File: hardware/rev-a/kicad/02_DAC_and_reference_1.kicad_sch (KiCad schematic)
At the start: 16 parts, among them U1 MCP4922-E/P, U2 MCP4922-E/P, U3 MCP4922-E/P, U4 MCP1501-20E/CHY

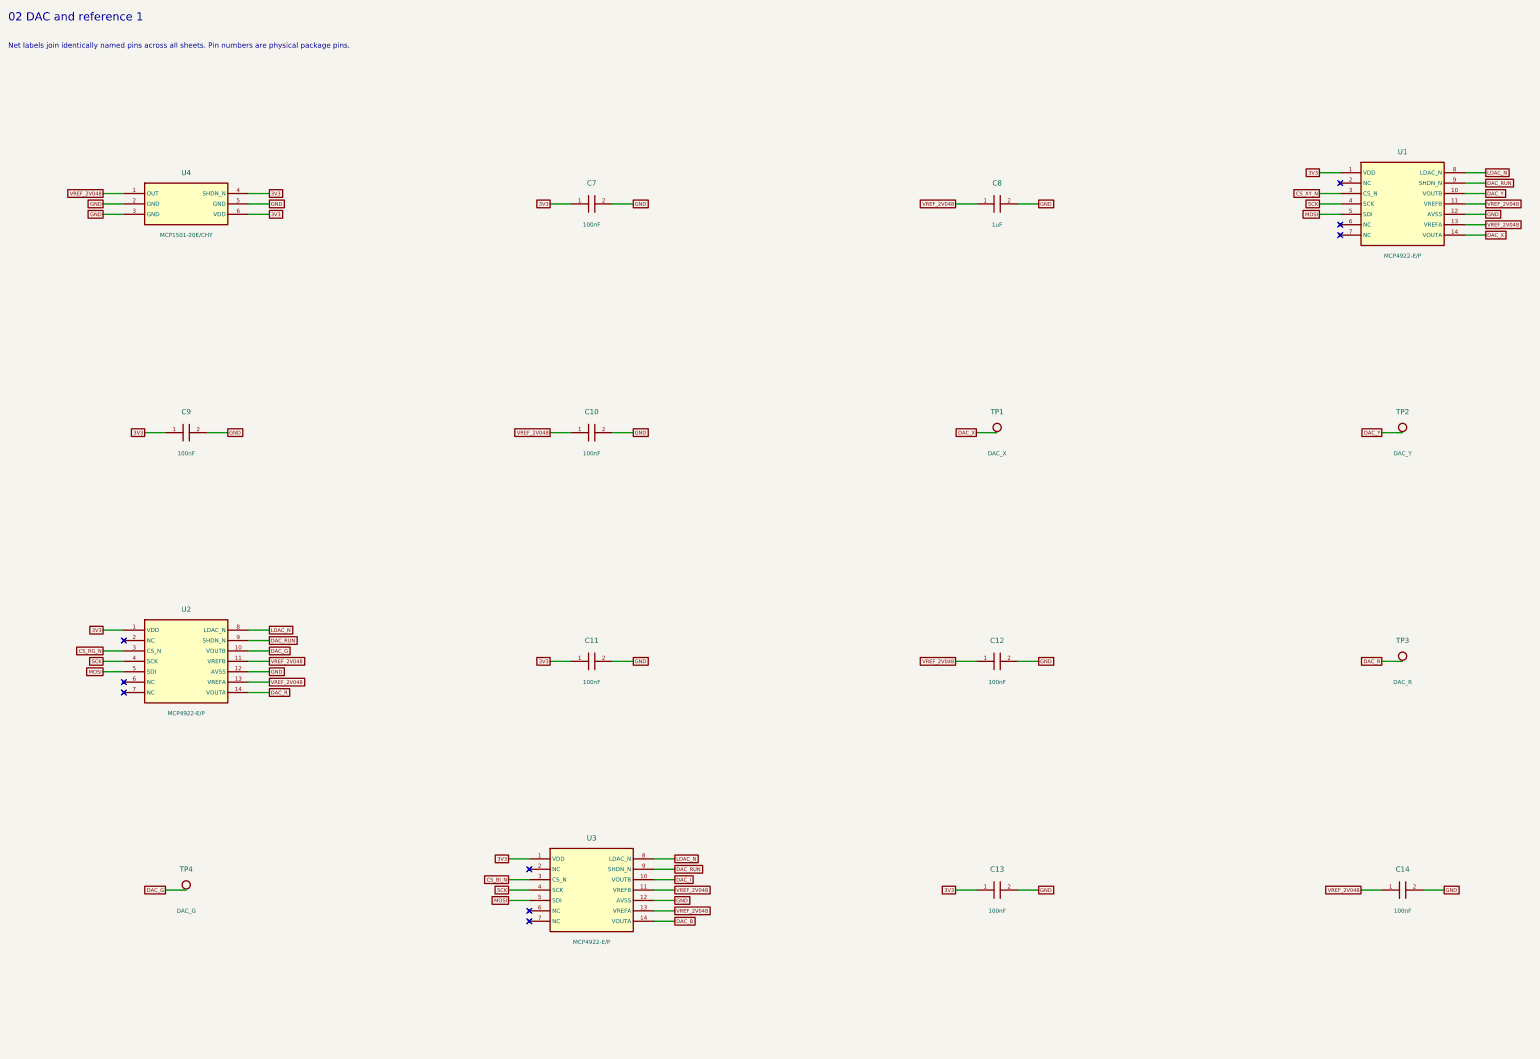
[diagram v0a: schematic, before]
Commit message: Redraw Rev.A schematics with functional blocks and explicit wiring
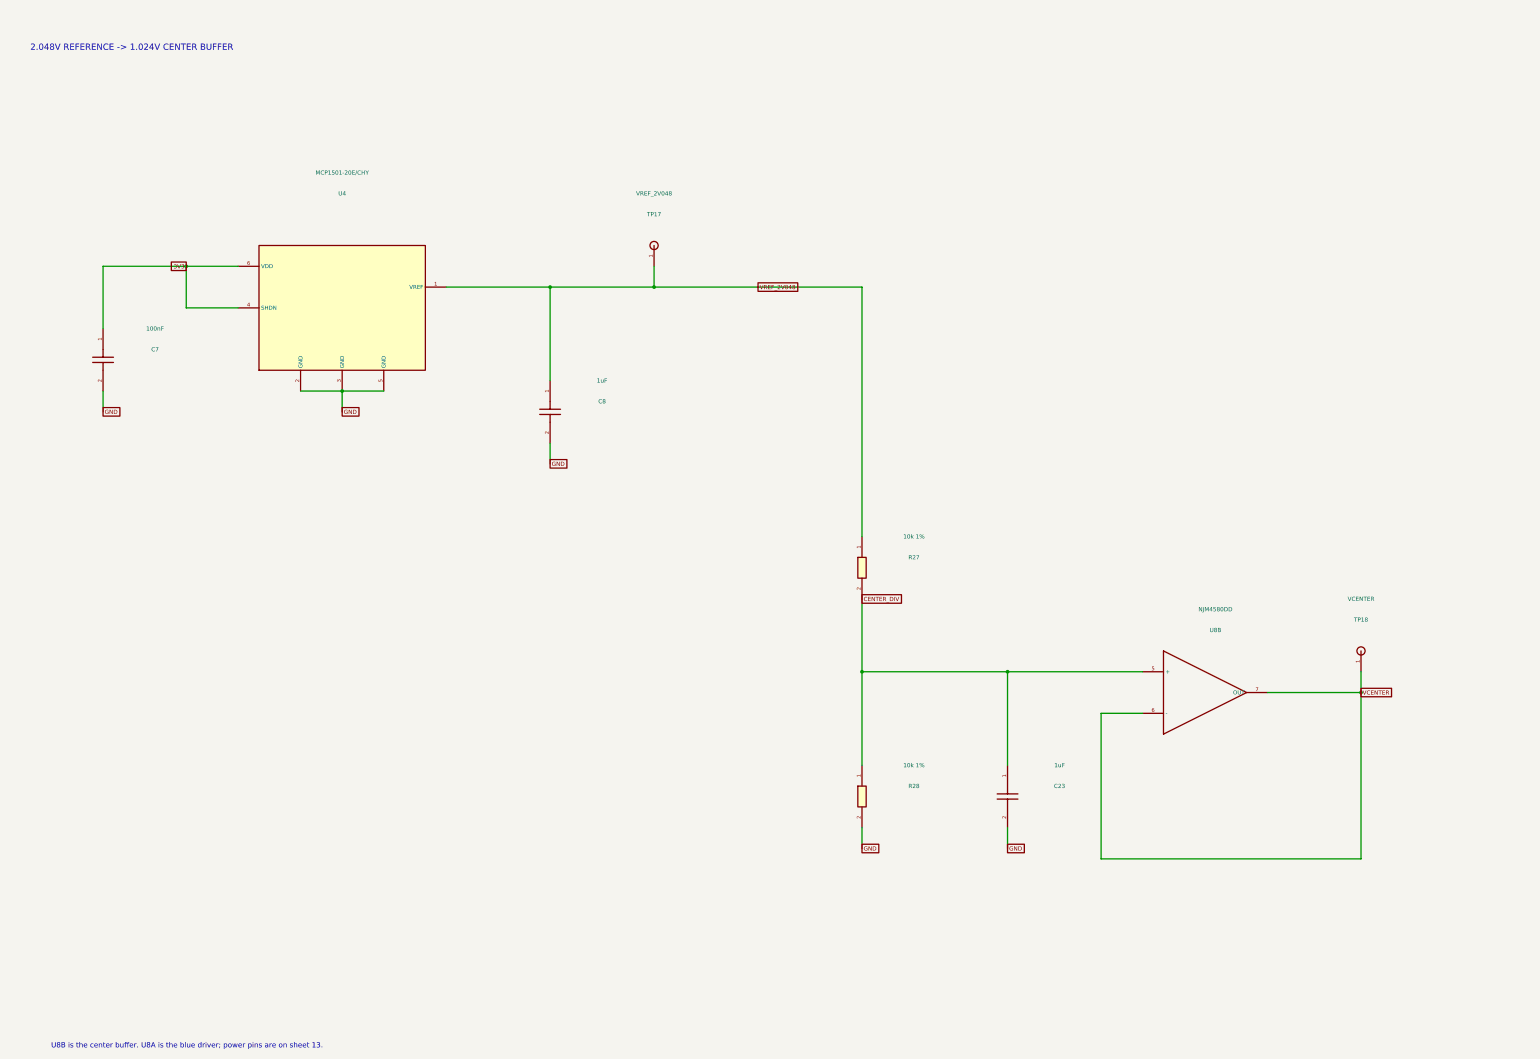
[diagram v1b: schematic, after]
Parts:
- removed C10, C11, C12, C13, C14, C9: 100nF, RevA:C_Disc_D5.0mm_W2.5mm_P5.00mm, symbol RevA:C
- removed TP1: DAC_X, RevA:TestPoint_THTPad_D2.0mm_Drill1.0mm, symbol RevA:TP
- removed TP2: DAC_Y, RevA:TestPoint_THTPad_D2.0mm_Drill1.0mm, symbol RevA:TP
- removed TP3: DAC_R, RevA:TestPoint_THTPad_D2.0mm_Drill1.0mm, symbol RevA:TP
- removed TP4: DAC_G, RevA:TestPoint_THTPad_D2.0mm_Drill1.0mm, symbol RevA:TP
- removed U1, U2, U3: MCP4922-E/P, RevA:DIP-14_W7.62mm, symbol RevA:DAC
- added C23: 1uF, RevA:C_Disc_D5.0mm_W2.5mm_P5.00mm, symbol RevA:C
- added R27, R28: 10k 1%, RevA:R_Axial_DIN0207_L6.3mm_D2.5mm_P10.16mm_Horizontal, symbol RevA:R
- added TP17: VREF_2V048, RevA:TestPoint_THTPad_D2.0mm_Drill1.0mm, symbol RevA:TP
- added TP18: VCENTER, RevA:TestPoint_THTPad_D2.0mm_Drill1.0mm, symbol RevA:TP
- added U8: NJM4580DD, RevA:DIP-8_W7.62mm, symbol RevA:AMP
- U4: symbol RevA:VREF -> RevA:Part_U4
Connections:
- net GND: now also C23.2, R28.2
- net VREF_2V048: now also R27.1, TP17.1
- new net CENTER_DIV: C23.1, R27.2, R28.1, U8.5 (+)
- new net VCENTER: TP18.1, U8.6 (-), U8.7 (OUT)
- no-connect marks 9 -> 0
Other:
- note added: "2.048V REFERENCE -> 1.024V CENTER BUFFER"
- note added: "U8B is the center buffer. U8A is the blue driver; power pins are on sheet 13."
- note removed: "02 DAC and reference 1"
- note removed: "Net labels join identically named pins across all sheets. Pin numbers are physical package pins."
- company: CoreS3 ILDA evaluation -> (none)
- title: 02_DAC_and_reference_1 -> 03 / Precision reference and XY center
- moved on the sheet: U4
